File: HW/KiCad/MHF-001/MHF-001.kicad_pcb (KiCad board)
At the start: 2 copper layers, 252.9 x 100.2 mm, 148 parts, among them J1 DE15_Socket_HighDensity_Mount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, J10 I2C, J11 5V, J12 Reset, J13 AREF, J14 XTAL2, J15 XTAL1, J16 AVCC, J17 SDcard, J18 RTC1, J19 RTC2, J2 Mini-DIN-6, J20 SDcardpins, J21 5V, J22 3.3V, J23 VIN 12V, J3 Conn_Coaxial, J4 Conn_02x32_Odd_Even, J5 USB_B_Micro, J6 02x32, J7 SPI, J8 AVR-ISP-6, J9 Serial, M3 CY7C109D-10ZXI, M5 CY7C109D-10ZXI, Q1 BC107, U1 ATMEGA2560-16AU, U10 74HC245, U11 74HC245, U12 74HC245, U13 CH340G, U14 AMS1117-5.0, U15 AMS1117-3.3, U2 74HC14, U3 74LS08, U4 74HC165, U6 74AHC373PW, U7 74HC595, U8 74HC595, U9 74HC157, Y1 16 MHz, Y2 12 MHz

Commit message: Final placement of parts (I hope)
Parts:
- removed J13: AREF, Connector_Wire:SolderWire-0.5sqmm_1x01_D0.9mm_OD2.1mm
- removed J14: XTAL2, Connector_Wire:SolderWire-0.5sqmm_1x01_D0.9mm_OD2.1mm
- removed J15: XTAL1, Connector_Wire:SolderWire-0.5sqmm_1x01_D0.9mm_OD2.1mm
- removed J16: AVCC, Connector_Wire:SolderWire-0.5sqmm_1x01_D0.9mm_OD2.1mm
- removed J18: RTC1, Connector_PinHeader_2.54mm:PinHeader_1x04_P2.54mm_Vertical
- removed J19: RTC2, Connector_PinHeader_2.54mm:PinHeader_1x06_P2.54mm_Vertical
- removed J21: 5V, Connector_PinHeader_2.54mm:PinHeader_1x02_P2.54mm_Vertical
- removed J22: 3.3V, Connector_PinHeader_2.54mm:PinHeader_1x02_P2.54mm_Vertical
- removed JP89, JP90, JP93: SolderJumper_2_Bridged, Jumper:SolderJumper-2_P1.3mm_Bridged_Pad1.0x1.5mm
- removed N4: ~, Gilhad:NetJoint
- added J24: AND_B1, Connector_Wire:SolderWire-0.5sqmm_1x01_D0.9mm_OD2.1mm, B.Cu at (103.8, 73.7)
- added J25: AND_B2, Connector_Wire:SolderWire-0.5sqmm_1x01_D0.9mm_OD2.1mm, B.Cu at (103.8, 76.1)
- added J26: AND_C1, Connector_Wire:SolderWire-0.5sqmm_1x01_D0.9mm_OD2.1mm, B.Cu at (106.9, 78.6)
- added J27: AND_C2, Connector_Wire:SolderWire-0.5sqmm_1x01_D0.9mm_OD2.1mm, B.Cu at (106.8, 76.1)
- added J28: AND_D1, Connector_Wire:SolderWire-0.5sqmm_1x01_D0.9mm_OD2.1mm, B.Cu at (106.8, 71.1)
- added J29: AND_D2, Connector_Wire:SolderWire-0.5sqmm_1x01_D0.9mm_OD2.1mm, B.Cu at (106.7, 68.6)
- added J30: AND_Dx, Connector_Wire:SolderWire-0.5sqmm_1x01_D0.9mm_OD2.1mm, B.Cu at (106.8, 73.6)
- added J31: AND_Cx, Connector_Wire:SolderWire-0.5sqmm_1x01_D0.9mm_OD2.1mm, B.Cu at (106.8, 81.1)
- added J32: AND_Bx, Connector_Wire:SolderWire-0.5sqmm_1x01_D0.9mm_OD2.1mm, B.Cu at (103.8, 78.7)
- added J33: NOTF, Connector_Wire:SolderWire-0.5sqmm_1x01_D0.9mm_OD2.1mm, B.Cu at (94.0, 96.5)
- added J34: NOTE, Connector_Wire:SolderWire-0.5sqmm_1x01_D0.9mm_OD2.1mm, B.Cu at (94.0, 91.4)
- added J35: NOTEx, Connector_Wire:SolderWire-0.5sqmm_1x01_D0.9mm_OD2.1mm, B.Cu at (94.0, 88.9)
- added J36: NOTFx, Connector_Wire:SolderWire-0.5sqmm_1x01_D0.9mm_OD2.1mm, B.Cu at (94.0, 94.0)
- added JP10: ANDD2+, Jumper:SolderJumper-2_P1.3mm_Bridged_Pad1.0x1.5mm, B.Cu at (111.2, 66.7)
- added JP11: NOTF, Jumper:SolderJumper-2_P1.3mm_Bridged_Pad1.0x1.5mm, B.Cu at (96.5, 96.5)
- added JP12: NOTE, Jumper:SolderJumper-2_P1.3mm_Bridged_Pad1.0x1.5mm, B.Cu at (96.5, 91.4)
- added JP5: ANDB1+, Jumper:SolderJumper-2_P1.3mm_Bridged_Pad1.0x1.5mm, B.Cu at (103.7, 70.4)
- added JP6: ANDB2+, Jumper:SolderJumper-2_P1.3mm_Bridged_Pad1.0x1.5mm, B.Cu at (111.8, 82.1)
- added JP7: ANDC1+, Jumper:SolderJumper-2_P1.3mm_Bridged_Pad1.0x1.5mm, B.Cu at (111.6, 79.4)
- added JP8: ANDC2+, Jumper:SolderJumper-2_P1.3mm_Bridged_Pad1.0x1.5mm, B.Cu at (115.0, 79.4)
- added JP9: ANDD1+, Jumper:SolderJumper-2_P1.3mm_Bridged_Pad1.0x1.5mm, B.Cu at (111.1, 69.8)
- added N1: ~, NetTie:NetTie-2_SMD_Pad0.5mm, F.Cu at (92.5, 33.9)
- C1: value 100 pF?? -> 100 pF
- C10, C11, C12, C13, C14, C15, C16, C2, C5, C6, C7, C8, C9, D2, D3, R12, R13, R16, R17, R18, R19, R20, R21, R22, R23, R25, R28, R29, R30, R31, R34, R35, R37, R38, U14, U15, Y1: moved to B.Cu
- J1: value DE15_Socket_HighDensity_MountingHoles -> VGA
- J11: value 5V -> + 5V -; footprint Connector_PinHeader_2.54mm:PinHeader_2x03_P2.54mm_Vertical -> Connector_PinSocket_2.54mm:PinSocket_2x03_P2.54mm_Vertical
- J2: value Mini-DIN-6 -> PS/2
- J3: value Conn_Coaxial -> RCA; footprint other.pretty:CUI_RCJ-047 -> Gilhad:CUI_RCJ-047_Yellow
- J4: value Conn_02x32_Odd_Even -> SysBus
- J5: value USB_B_Micro -> Micro
- J6: value 02x32 -> SysBus
- J8: value AVR-ISP-6 -> ISP
- JP1: value SolderJumper_2_Bridged -> MISO
- JP100: value SolderJumper_3_Open -> SHRequest
- JP102: value SolderJumper_3_Open -> S_Enable
- JP103: value SolderJumper_3_Open -> S_Read
- JP104: value SolderJumper_3_Open -> SWrt
- JP105: value SolderJumper_3_Open -> GDd
- JP106: value SolderJumper_3_Open -> GEn
- JP107: value SolderJumper_3_Open -> GAD
- JP2: value SolderJumper_2_Bridged -> MOSI
- JP3: value SolderJumper_2_Bridged -> SCK
- JP4: value SolderJumper_2_Bridged -> SS
- JP55: value SolderJumper_2_Bridged -> PS2_Data; footprint Jumper:SolderJumper-2_P1.3mm_Bridged_Pad1.0x1.5mm -> Jumper:SolderJumper-2_P1.3mm_Open_RoundedPad1.0x1.5mm
- JP56: value SolderJumper_2_Bridged -> PS2_CLK; footprint Jumper:SolderJumper-2_P1.3mm_Bridged_Pad1.0x1.5mm -> Jumper:SolderJumper-2_P1.3mm_Open_RoundedPad1.0x1.5mm
- JP91: value SolderJumper_2_Bridged -> Inside
- JP92: value SolderJumper_3_Open -> X16
- JP94: value SolderJumper_3_Open -> A_HALT
- JP95: value SolderJumper_3_Open -> A_READ
- JP98: value SolderJumper_3_Open -> SHDirty
- JP99: value SolderJumper_3_Open -> SHGranted
- LED1: value LED -> RX
- LED2: value LED -> TX
- LED3: value LED -> ON
- LED4: value LED -> CTS
- LED5: value LED -> RTS
- LED6: value LED -> SCL
- N3: footprint Gilhad:NetJoint -> NetTie:NetTie-2_SMD_Pad0.5mm
- PA1: value Conn_01x08 -> PA
- PB1: value Conn_01x08 -> PB
- PC1: value Conn_01x08 -> PC
- PD1: value Conn_01x08 -> PD
- PE1: value Conn_01x08 -> PE
- PF1: value Conn_01x08 -> PF
- PG1: value Conn_01x06 -> PG
- PH1: value Conn_01x08 -> PH
- PJ1: value Conn_01x08 -> PJ
- PK1: value Conn_01x08 -> PK
- PL1: value Conn_01x08 -> PL
- R1: value 3k3 -> 3k3/22k
- R32, R33: value --- -> 4k7; moved to B.Cu
- S1: value TS06-667-30-BK-100-G-SMT-TR -> Reset
- U1: value ATMEGA2560-16AU -> ATMEGA2560
- U6: value 74AHC373PW -> 74AHC373
- moved J17 189.3 mm to (59.3, 87.0), turned to 90 degrees
- moved J20 186.2 mm to (59.3, 81.9), turned to 90 degrees
- moved JP4 184.8 mm to (59.3, 79.4), turned to 90 degrees
- moved JP3 181.5 mm to (61.9, 79.4), turned to 90 degrees
- moved JP2 178.2 mm to (64.4, 79.4), turned to 90 degrees
- moved JP1 174.9 mm to (67.0, 79.4), turned to 90 degrees
- moved H5 157.0 mm to (29.3, 31.7)
- moved H6 157.0 mm to (119.4, 31.7)
- moved H7 157.0 mm to (119.4, 121.7)
- moved H8 157.0 mm to (29.4, 121.7)
- moved J4 157.0 mm to (30.2, 37.4)
- moved J6 157.0 mm to (35.3, 37.4)
- moved U3 147.9 mm to (101.6, 66.0)
- moved R40 147.2 mm to (105.2, 41.2), turned to 90 degrees
- moved R5 145.6 mm to (103.1, 63.4)
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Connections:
- net /Clock renamed Net-(J2-Pad5)
- D1 pad 1: Net-(D1-K) -> PS2 Clock
- J2 pad 1: /Data -> PS2 Data
- N3 pad 1: VGA data 3 -> ~{SUPRESS}
- N3 pad 2: ~{SUPRESS} -> VGA data 3
- R1 pad 2: Net-(D1-K) -> PS2 Clock
- R12 pad 1: /Data -> PS2 Data
- U1 pad 100: Net-(J16-Pin_1) -> +5V
- U2 pad 10: unconnected-(U2-Pad10) -> Net-(J35-Pin_1)
- U2 pad 11: Net-(U2-Pad11) -> Net-(J34-Pin_1)
- U2 pad 12: Net-(U2-Pad11) -> Net-(J36-Pin_1)
- U2 pad 13: GND -> Net-(J33-Pin_1)
- U2 pad 4: Net-(D1-K) -> PS2 Clock
- U3 pad 10: Net-(U3-Pad10) -> Net-(J27-Pin_1)
- U3 pad 11: Net-(U3-Pad10) -> Net-(J30-Pin_1)
- U3 pad 12: GND -> Net-(J28-Pin_1)
- U3 pad 13: GND -> Net-(J29-Pin_1)
- U3 pad 4: Net-(U3-Pad4) -> Net-(J24-Pin_1)
- U3 pad 5: Net-(U3-Pad4) -> Net-(J25-Pin_1)
- U3 pad 6: unconnected-(U3-Pad6) -> Net-(J32-Pin_1)
- U3 pad 8: Net-(U3-Pad4) -> Net-(J31-Pin_1)
- U3 pad 9: Net-(U3-Pad10) -> Net-(J26-Pin_1)
- U7 pad 12: Net-(D1-K) -> PS2 Clock
- U7 pad 14: /Data -> PS2 Data
- U8 pad 12: Net-(D1-K) -> PS2 Clock
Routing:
- net GND: track 53.6 -> 180.9 mm, vias 1 -> 3
- net +5V: track 10.1 -> 81.5 mm, vias 1 -> 2
- net Red: track 0.00 -> 27.3 mm, vias 0 -> 1
- net unconnected-(J1-Pad0): track 25.8 -> 1.41 mm
- net Green: track 0.00 -> 21.5 mm, vias 0 -> 1
- net Net-(J25-Pin_1): track 0.00 -> 15.9 mm, vias 0 -> 1
- net Blue: track 0.00 -> 14.7 mm, vias 0 -> 1
- net A16: track 0.00 -> 12.9 mm
- net A_HALT: track 0.00 -> 12.9 mm
- net A_READ: track 0.00 -> 12.6 mm
- net Net-(U9-Zc): track 0.00 -> 12.2 mm
- net B_READ: track 0.00 -> 12.1 mm
- net B16: track 0.00 -> 12.1 mm
- net B_HALT: track 0.00 -> 12.1 mm
- net +3.3V: track 0.00 -> 12.1 mm
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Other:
- board size 252.9 x 100.2 mm -> 99.9 x 99.9 mm

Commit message: WayWayWay and other final touches
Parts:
- added J13: +5V, Connector_Wire:SolderWire-0.5sqmm_1x01_D0.9mm_OD2.1mm, F.Cu at (81.4, 39.1)
- added J14: GND, Connector_Wire:SolderWire-0.5sqmm_1x01_D0.9mm_OD2.1mm, F.Cu at (77.7, 39.1)
- added JP13: Xhalt, Jumper:SolderJumper-2_P1.3mm_Bridged_Pad1.0x1.5mm, F.Cu at (104.0, 59.7)
- added LED7: SPI, LED_SMD:LED_0805_2012Metric, F.Cu at (56.4, 81.7)
- added LED8: HALT, LED_SMD:LED_0805_2012Metric, F.Cu at (122.1, 64.5)
- added R41: 1k, Resistor_SMD:R_0805_2012Metric_Pad1.20x1.40mm_HandSolder, B.Cu at (56.2, 81.9)
- added R42: 1k, Resistor_SMD:R_0603_1608Metric_Pad0.98x0.95mm_HandSolder, B.Cu at (105.2, 32.6)
- added R43: 1k, Resistor_SMD:R_0805_2012Metric_Pad1.20x1.40mm_HandSolder, B.Cu at (122.0, 64.5)
- F1, R40: moved to B.Cu
- J11: value + 5V - -> - 5V +
- JP104: value SWrt -> S_Write
- JP105: value GDd -> GDdir
- JP106: value GEn -> GEnable
- JP107: value GAD -> GADir
- JP12: value NOTE -> HaltLED
- PA1: value PA -> PA0
- PB1: value PB -> PB0
- PC1: value PC -> PC0
- PD1: value PD -> PD0
- PE1: value PE -> PE0
- PF1: value PF -> PF0
- PG1: value PG -> PG0
- PH1: value PH -> PH0
- PJ1: value PJ -> PJ0
- PK1: value PK -> PK0
- PL1: value PL -> PL0
- moved PA1 17.9 mm to (73.1, 40.0), turned to -90 degrees
- moved JP12 10.5 mm to (96.6, 81.0), turned to 0 degrees
- moved PJ1 9.84 mm to (55.3, 46.5)
- moved JP6 7.97 mm to (103.9, 81.4), turned to 90 degrees
- moved PF1 2.71 mm to (52.4, 29.0)
- moved U7 2.68 mm to (81.4, 83.9)
- moved U8 2.68 mm to (81.4, 105.5)
- moved R17 2.68 mm to (86.5, 108.0)
- moved R16 2.68 mm to (84.0, 105.5)
- moved R19 2.68 mm to (84.0, 96.6)
- moved R21 2.68 mm to (84.0, 91.5)
- moved R23 2.68 mm to (84.0, 86.5)
- moved R18 2.68 mm to (84.0, 99.2)
- moved R20 2.68 mm to (84.0, 94.1)
- moved R22 2.68 mm to (84.0, 89.0)
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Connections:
- JP12 pad 1: +5V -> Net-(JP12-A)
- PE1 pad 6: X_HALT -> Net-(JP12-A)
- U1 pad 7: X_HALT -> Net-(JP12-A)
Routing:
- net XAD4: track 13.5 -> 0.00 mm, vias 1 -> 0
- net XAD5: track 13.5 -> 0.00 mm, vias 1 -> 0
- net A16: track 12.9 -> 0.00 mm
- net XAD6: track 12.9 -> 0.00 mm, vias 1 -> 0
- net A_HALT: track 12.9 -> 0.00 mm
- net XAD7: track 12.8 -> 0.00 mm, vias 1 -> 0
- net A_READ: track 12.6 -> 0.00 mm
- net B_READ: track 12.1 -> 0.00 mm
- net B16: track 12.1 -> 0.00 mm
- net B_HALT: track 12.1 -> 0.00 mm
- net GND: track 180.9 -> 170.3 mm, vias 3 -> 2
- net Net-(J1-Pad13): track 10.8 -> 0.77 mm, vias 1 -> 0
- net Net-(J1-Pad14): track 10.7 -> 0.79 mm, vias 1 -> 0
- net Net-(M3-A0): track 9.49 -> 0.00 mm, vias 1 -> 0
- net +5V: track 81.5 -> 72.5 mm, vias 2 -> 1
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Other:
- board text added: "+5V"
- board text added: "AND"
- board text added: "CTS"
- board text added: "GND"
- board text added: "Gilhad@seznam.cz 13.07.2025"
- board text added: "MHF-001"
- board text added: "MOSI"
- board text added: "NOT"
- board text added: "RTS"
- board text added: "RX"
- board text added: "Reset"
- board text added: "SCK"
- board text added: "TX"
- board text added: "WayWayWay"
- board text added: "https://github.com/githubgilhad/MegaHomeFORTH"
- board text added: "up-HALT-dn"

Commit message: condensators
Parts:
- added Cx1: Cx, Capacitor_THT:C_Disc_D3.0mm_W2.0mm_P2.50mm, F.Cu at (88.7, 79.8)
- added Cx10: Cx, Capacitor_THT:C_Disc_D3.0mm_W2.0mm_P2.50mm, F.Cu at (37.5, 33.1)
- added Cx11: Cx, Capacitor_THT:C_Disc_D3.0mm_W2.0mm_P2.50mm, F.Cu at (51.9, 47.5)
- added Cx12: Cx, Capacitor_THT:C_Disc_D3.0mm_W2.0mm_P2.50mm, F.Cu at (47.7, 76.8)
- added Cx13: Cx, Capacitor_THT:C_Disc_D3.0mm_W2.0mm_P2.50mm, F.Cu at (38.0, 63.1)
- added Cx14: Cx, Capacitor_THT:CP_Radial_D5.0mm_P2.50mm, F.Cu at (80.6, 43.4)
- added Cx15: Cx, Capacitor_THT:CP_Radial_D5.0mm_P2.50mm, F.Cu at (75.5, 75.2)
- added Cx2: Cx, Capacitor_THT:C_Disc_D3.0mm_W2.0mm_P2.50mm, F.Cu at (85.9, 124.9)
- added Cx3: Cx, Capacitor_THT:C_Disc_D3.0mm_W2.0mm_P2.50mm, F.Cu at (91.7, 120.1)
- added Cx4: Cx, Capacitor_THT:C_Disc_D3.0mm_W2.0mm_P2.50mm, F.Cu at (96.6, 80.9)
- added Cx5: Cx, Capacitor_THT:C_Disc_D3.0mm_W2.0mm_P2.50mm, F.Cu at (109.3, 62.9)
- added Cx6: Cx, Capacitor_THT:C_Disc_D3.0mm_W2.0mm_P2.50mm, F.Cu at (107.6, 56.1)
- added Cx7: Cx, Capacitor_THT:C_Disc_D3.0mm_W2.0mm_P2.50mm, F.Cu at (96.5, 49.2)
- added Cx8: Cx, Capacitor_THT:C_Disc_D3.0mm_W2.0mm_P2.50mm, F.Cu at (72.1, 44.1)
- added Cx9: Cx, Capacitor_THT:C_Disc_D3.0mm_W2.0mm_P2.50mm, F.Cu at (61.0, 55.6)
- J11: value - 5V + -> + 5V -
- moved R4 7.82 mm to (103.3, 56.2)
- moved C5 7.78 mm to (91.8, 57.1), turned to 45 degrees
- moved C6 6.48 mm to (89.5, 54.4), turned to 135 degrees
- moved JP13 5.80 mm to (98.8, 57.3), turned to -90 degrees
- moved C8 5.72 mm to (86.2, 63.5), turned to 45 degrees
- moved JP12 5.55 mm to (97.6, 75.5), turned to 90 degrees
- moved C13 4.93 mm to (85.8, 52.7), turned to -135 degrees
- moved Y1 3.68 mm to (80.5, 52.9), turned to 45 degrees
- moved U1 2.44 mm to (84.8, 56.9), turned to -135 degrees
- moved C7 2.30 mm to (81.7, 60.6), turned to -45 degrees
- moved M3 2.20 mm to (66.6, 54.2)
- moved R29 2.12 mm to (83.2, 55.3), turned to -135 degrees
- moved PH1 1.91 mm to (96.5, 124.6)
- moved U6 1.89 mm to (66.7, 55.6)
- moved PG1 1.51 mm to (73.7, 30.2)
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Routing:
- net +5V: track 72.5 -> 357.9 mm, vias 1 -> 5
- net GND: track 170.3 -> 368.1 mm, vias 2 -> 6
- net AREF: track 0.00 -> 3.00 mm, vias 0 -> 1
- net Net-(Q1-B): track 2.93 -> 0.00 mm
- net Red: track 27.3 -> 29.8 mm

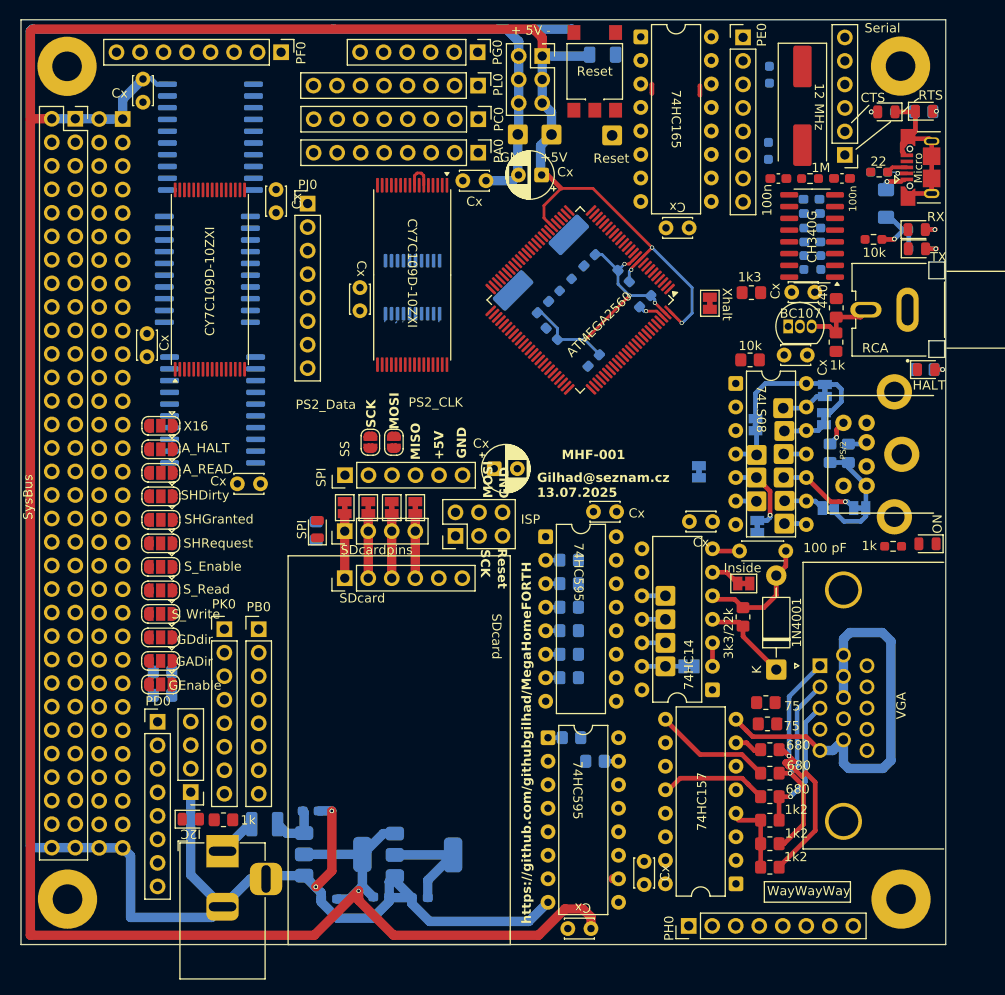
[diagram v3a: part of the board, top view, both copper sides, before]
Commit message: XTALs, AVCC, AREF
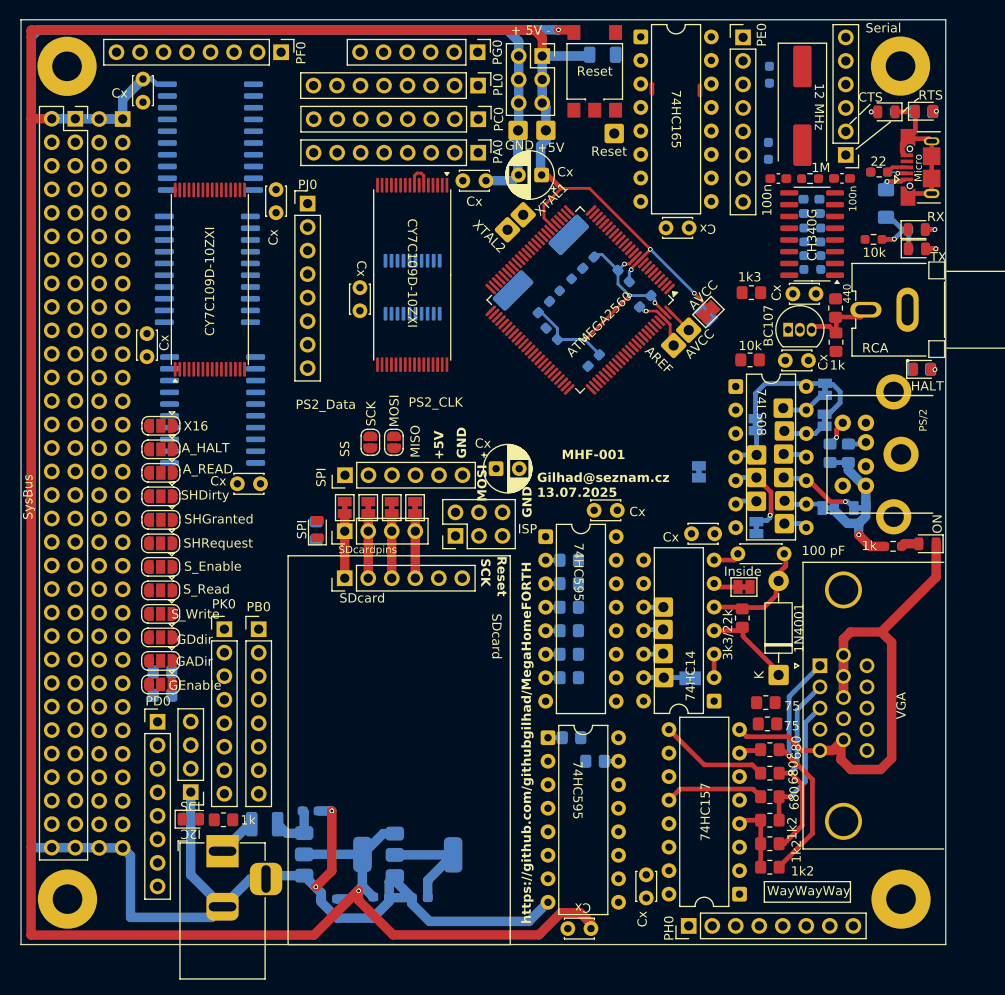
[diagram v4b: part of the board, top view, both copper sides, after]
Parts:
- added J15: AREF, Gilhad:PinHole_1x01_2.54xrectangle, F.Cu at (94.9, 61.9)
- added J16: XTAL2, Gilhad:PinHole_1x01_2.54xrectangle, F.Cu at (76.9, 49.4)
- added J18: XTAL1, Gilhad:PinHole_1x01_2.54xrectangle, F.Cu at (78.6, 47.7)
- added J19: AVCC, Gilhad:PinHole_1x01_2.54xrectangle, F.Cu at (96.5, 60.2)
- added JP14: AVCC, Jumper:SolderJumper-2_P1.3mm_Bridged_Pad1.0x1.5mm, F.Cu at (98.6, 58.3)
- J12, J13, J14, J24, J25, J26, J27, J28, J29, J30, J31, J32, J33, J34, J35, J36: footprint Connector_Wire:SolderWire-0.5sqmm_1x01_D0.9mm_OD2.1mm -> Gilhad:PinHole_1x01_2.54xrectangle
- JP13: moved to B.Cu
- moved Cx3 1.47 mm to (91.9, 121.5)
- moved Cx4 1.34 mm to (96.8, 82.2)
- moved JP13 1.33 mm to (98.4, 58.6), turned to -45 degrees
- moved JP11 1.30 mm to (96.6, 97.8)
- moved J35 1.24 mm to (93.8, 90.1)
- moved J33 1.23 mm to (93.8, 97.7)
- moved U2 1.23 mm to (99.2, 100.3)
- moved J36 1.19 mm to (93.7, 95.1)
- moved U9 1.18 mm to (102.0, 121.1)
- moved J34 1.12 mm to (93.7, 92.5)
- moved J13 0.76 mm to (81.1, 38.6)
- moved D1 0.64 mm to (106.2, 97.5)
- moved Cx5 0.60 mm to (109.4, 63.5)
- moved J14 0.43 mm to (78.1, 38.6)
- moved LED8 0.43 mm to (121.7, 64.4)
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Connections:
- U1 pad 100: +5V -> Net-(J19-Pin_1)
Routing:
- net GND: track 368.1 -> 382.5 mm, vias 6 -> 7
- net AREF: track 3.00 -> 6.51 mm
- net Net-(J19-Pin_1): track 0.00 -> 2.94 mm
- net Red: track 29.8 -> 27.1 mm
- net /L-on: track 0.00 -> 1.98 mm
- net +5V: track 357.9 -> 356.5 mm, vias 5 -> 6
- net Net-(LED8-A): track 1.75 -> 0.78 mm
- net Net-(U9-Zd): track 11.6 -> 10.7 mm
- net Net-(J28-Pin_1): track 4.50 -> 5.13 mm
- net Net-(U9-Zc): track 12.5 -> 11.9 mm
- net Net-(U9-Zb): track 3.05 -> 2.43 mm
- net Net-(D1-A): track 12.8 -> 12.2 mm

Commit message: Autorouting
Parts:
- moved Cx7 0.13 mm to (96.5, 49.3)
- moved U4 0.11 mm to (91.3, 28.6)
- moved R3 0.09 mm to (112.4, 61.6)
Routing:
- net GND: track 382.5 -> 847.1 mm, vias 7 -> 11
- net +5V: track 356.5 -> 740.4 mm, vias 6 -> 11
- net Shared_data_D1: track 0.00 -> 148.1 mm
- net HSyncVGA: track 0.00 -> 147.4 mm, vias 0 -> 2
- net VGA Latch: track 0.00 -> 139.4 mm, vias 0 -> 2
- net Reset: track 0.00 -> 125.3 mm, vias 0 -> 3
- net X16: track 0.00 -> 125.2 mm, vias 0 -> 2
- net PS2-OE: track 0.00 -> 120.4 mm, vias 0 -> 1
- net Shared_Address_A10: track 0.00 -> 120.1 mm, vias 0 -> 2
- net SIGNAL_RCA: track 0.00 -> 116.9 mm, vias 0 -> 2
- net SCL: track 0.00 -> 114.4 mm, vias 0 -> 1
- net Rf: track 0.00 -> 107.2 mm, vias 0 -> 4
- net Shared_data_D6: track 0.00 -> 104.9 mm, vias 0 -> 2
- net VSyncVGA: track 0.00 -> 103.2 mm, vias 0 -> 1
- net Shared_data_D5: track 0.00 -> 101.8 mm, vias 0 -> 2
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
